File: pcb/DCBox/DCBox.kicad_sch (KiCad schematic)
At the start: 36 parts, among them J1 DC-IN, J2 Out-1, J3 Out-2, J4 Out-3, U1 STC8H1K08_TSSOP20

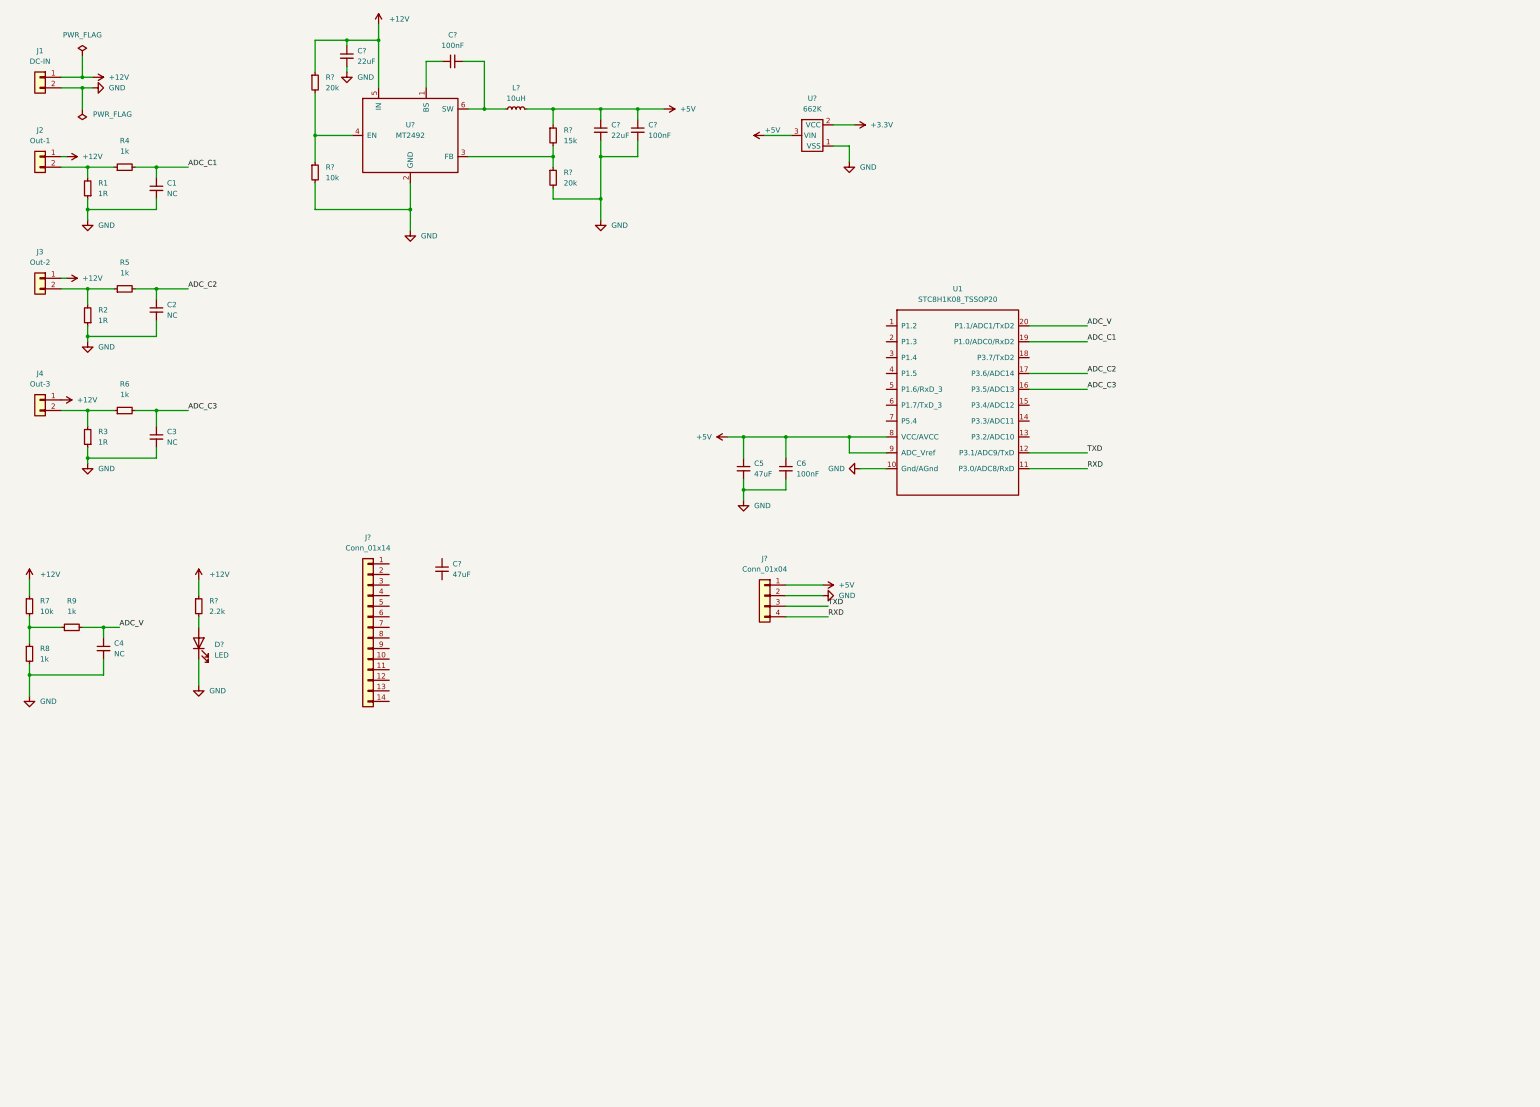
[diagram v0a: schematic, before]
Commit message: 1. 完善原理图 2. 添加显示屏datasheet
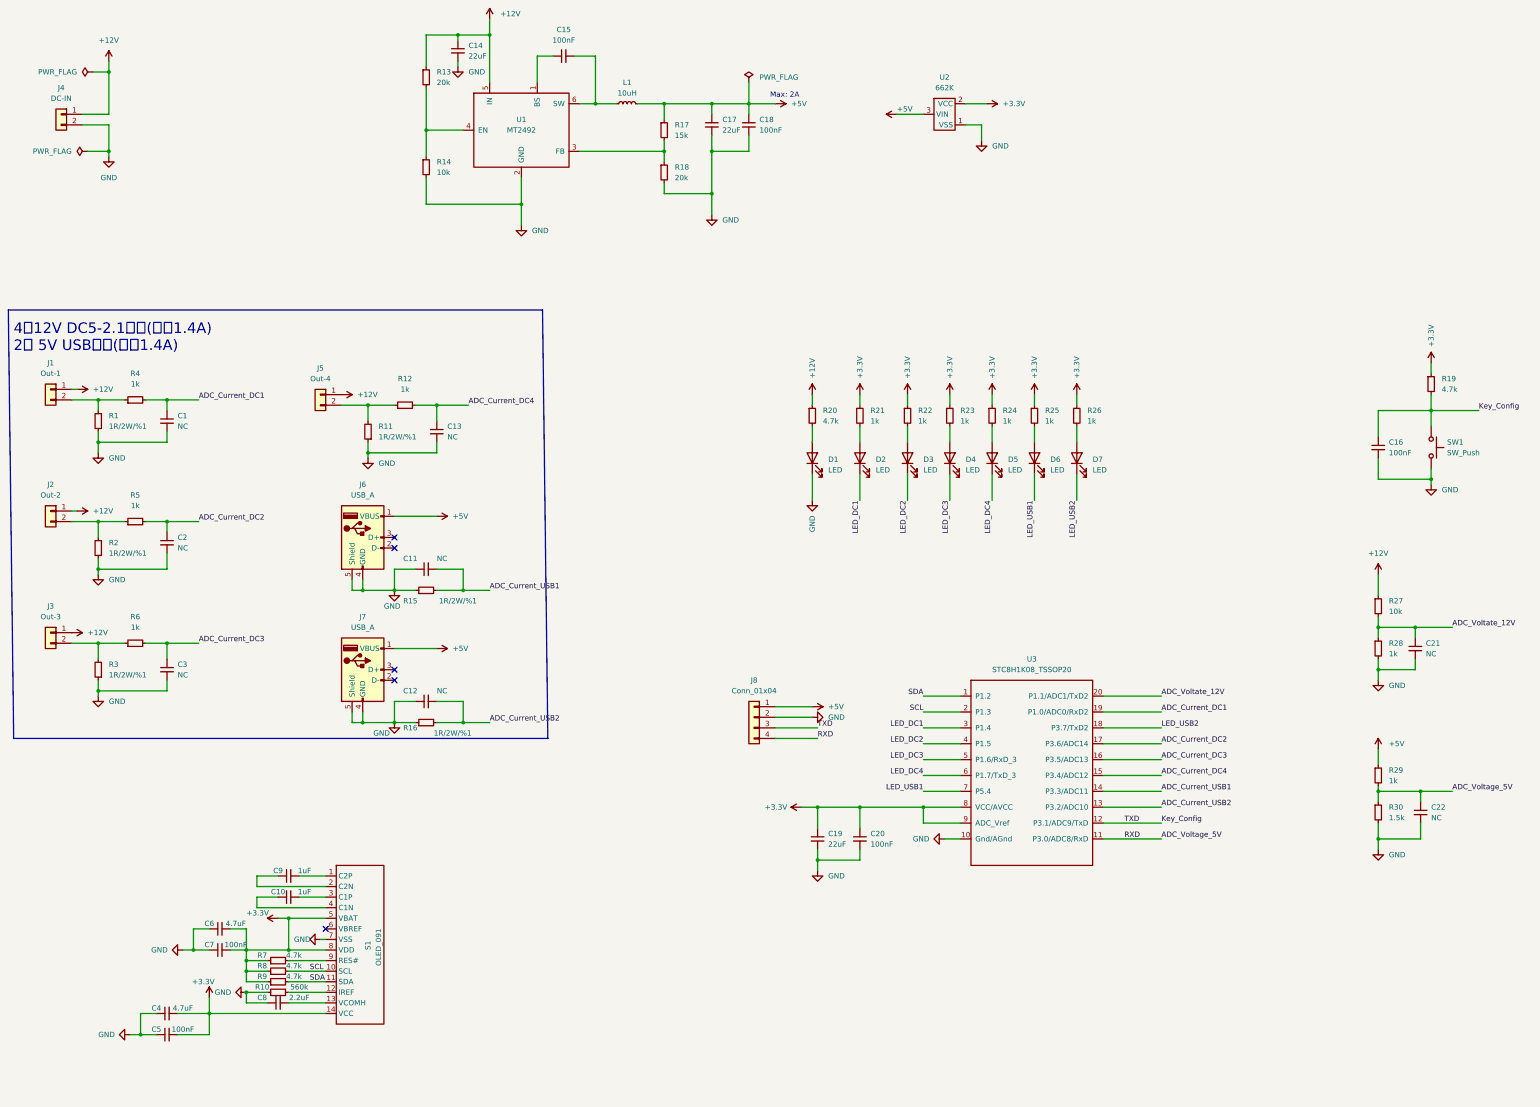
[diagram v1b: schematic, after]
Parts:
- removed C?: 47uF, symbol Device:C_Small
- removed D?: LED, symbol Device:LED
- removed J?: Conn_01x14, symbol Connector_Generic:Conn_01x14
- removed R?: 2.2k, symbol Device:R_Small
- added C10, C9: 1uF, symbol Device:C_Small
- added C11, C12, C13, C21, C22: NC, symbol Device:C_Small
- added C16, C5, C7: 100nF, symbol Device:C_Small
- added C6: 4.7uF, symbol Device:C_Small
- added C8: 2.2uF, symbol Device:C_Small
- added D1, D2, D3, D4, D5, D6, D7: LED, symbol Device:LED
- added J5: Out-4, jld:DC005, symbol Connector_Generic:Conn_01x02
- added J6, J7: USB_A, symbol Connector:USB_A
- added R10: 560k, symbol Device:R_Small
- added R11, R15, R16: 1R/2W/%1, lc_lib:2512_R, symbol Device:R_Small
- added R12, R21, R22, R23, R24, R25, R26, R28, R29: 1k, symbol Device:R_Small
- added R19, R20: 4.7k, symbol Device:R_Small
- added R27: 10k, symbol Device:R_Small
- added R30: 1.5k, symbol Device:R_Small
- added S1: OLED_091, symbol jld:OLED_091
- added SW1: SW_Push, symbol Switch:SW_Push
- C19: renamed from C5; value 47uF -> 22uF
- C4: value NC -> 4.7uF
- R1, R2, R3: value 1R -> 1R/2W/%1
- R7: value 10k -> 4.7k
- R8, R9: value 1k -> 4.7k
- gave numbers to parts that had none: 12
- renumbered C6 to C20, J2 to J1, J3 to J2, J4 to J3, J1 to J4, U1 to U3
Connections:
- net +12V: now also J5.1 (Pin_1), R20.1, R27.1; no longer R7.1
- net +3V3: now also C19.1, C20.1, C4.2, R7.1, R8.1, R9.1, U3.8 (VCC/AVCC), U3.9 (ADC_Vref), C5.2, C6.2, C7.2, R19.1, R21.1, R22.1, R23.1, R24.1, R25.1, R26.1, S1.14 (VCC), S1.5 (VBAT), S1.8 (VDD)
- net +5V: now also J6.1 (VBUS), J7.1 (VBUS), R29.1; no longer C19.1, C20.1, U3.8 (VCC/AVCC), U3.9 (ADC_Vref)
- net GND: now also C4.1, C11.1, C12.1, C13.2, C16.2, C21.2, C22.2, C5.1, C6.1, C7.1, C8.1, D1.1 (K), J6.4 (GND), J6.5 (Shield), J7.4 (GND), J7.5 (Shield), R10.1, R11.1, R15.1, R16.1, R28.2, R30.2, S1.7 (VSS), SW1.2; no longer C4.2, R8.2
- net SDA: now reaches U3.1 (P1.2)
- net SDA: now also R9.2, S1.11 (SDA)
- net ADC_Current_USB2: now reaches U3.13 (P3.2/ADC10)
- net ADC_Current_USB2: now also C12.2, R16.2
- net ADC_Current_USB1: now reaches U3.14 (P3.3/ADC11)
- net ADC_Current_USB1: now also C11.2, R15.2
- net ADC_Current_DC4: now reaches U3.15 (P3.4/ADC12)
- net ADC_Current_DC4: now also C13.1, R12.2
- net LED_USB2: now reaches U3.18 (P3.7/TxD2)
- net LED_USB2: now also D7.1 (K)
- net SCL: now reaches U3.2 (P1.3)
- net SCL: now also R8.2, S1.10 (SCL)
- net LED_DC1: now reaches U3.3 (P1.4)
- net LED_DC1: now also D2.1 (K)
- net LED_DC2: now reaches U3.4 (P1.5)
- net LED_DC2: now also D3.1 (K)
- net LED_DC3: now reaches U3.5 (P1.6/RxD_3)
- net LED_DC3: now also D4.1 (K)
- net LED_DC4: now reaches U3.6 (P1.7/TxD_3)
- net LED_DC4: now also D5.1 (K)
- net LED_USB1: now reaches U3.7 (P5.4)
- net LED_USB1: now also D6.1 (K)
- net ADC_C1 renamed ADC_Current_DC1
- net ADC_C2 renamed ADC_Current_DC2
- net ADC_C3 renamed ADC_Current_DC3
- removed net ADC_V: C4.1, R9.2, U3.20 (P1.1/ADC1/TxD2)
- net RXD renamed ADC_Voltage_5V
- net ADC_Voltage_5V: now also C22.1, R29.2, R30.1
- net TXD renamed Key_Config
- net Key_Config: now also C16.1, R19.2, SW1.1
- new net: R7.2, S1.9 (RES#)
- new net: D2.2 (A), R21.2
- new net: J5.2 (Pin_2), R11.2, R12.1
- new net: D4.2 (A), R23.2
- new net: D7.2 (A), R26.2
- new net: D1.2 (A), R20.2
- new net: D6.2 (A), R25.2
- new net: C8.2, S1.13 (VCOMH)
- new net: C9.2, S1.1 (C2P)
- new net: R10.2, S1.12 (IREF)
- new net: C9.1, S1.2 (C2N)
- new net: C10.2, S1.3 (C1P)
- new net: C10.1, S1.4 (C1N)
- new net: D3.2 (A), R22.2
- new net: D5.2 (A), R24.2
- new net ADC_Voltate_12V: C21.1, R27.2, R28.1, U3.20 (P1.1/ADC1/TxD2)
- no-connect marks 0 -> 5
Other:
- note added: "4路12V DC5-2.1输出(最大1.4A) 2路 5V USB输出(最大1.4A)"
- note added: "Max: 2A"
- moved on the sheet: C1, C14, C15, C17, C18, C19, C2, C20, C3, J1, J2, J3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

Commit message: 1. 完善布局
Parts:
- C1, C10, C11, C12, C13, C15, C16, C18, C2, C20, C21, C22, C3, C4, C5, C6, C7, C8, C9, R10, R12, R13, R14, R17, R18, R19, R20, R21, R22, R23, R24, R25, R26, R27, R28, R29, R30, R4, R5, R6, R7, R8, R9: footprint (none) -> lc_lib:0603_R
- C14, C17, C19: footprint (none) -> lc_lib:1206_R
- D1, D2, D3, D4, D5, D6, D7: footprint (none) -> lc_lib:0603_LED_N1
- J6, J7: footprint (none) -> Connector_USB:USB_A_Wuerth_614004134726_Horizontal
- J8: footprint (none) -> Connector_PinHeader_2.54mm:PinHeader_1x04_P2.54mm_Vertical
- SW1: footprint (none) -> jld:Button_SW_THT_6.2x6.2
- U1: footprint (none) -> lc_lib:SOT-23-6
- U2: footprint (none) -> lc_lib:SOT-23-3L
- U3: footprint (none) -> lc_lib:TSSOP-20
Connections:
- net ADC_Current_USB1: now also C11.1, J6.4 (GND), J6.5 (Shield), R15.1; no longer C11.2, R15.2
- net ADC_Current_USB2: now also C12.1, J7.4 (GND), J7.5 (Shield), R16.1; no longer C12.2, R16.2
- net GND: now also C11.2, C12.2, R15.2, R16.2; no longer C11.1, C12.1, J6.4 (GND), J6.5 (Shield), J7.4 (GND), J7.5 (Shield), R15.1, R16.1

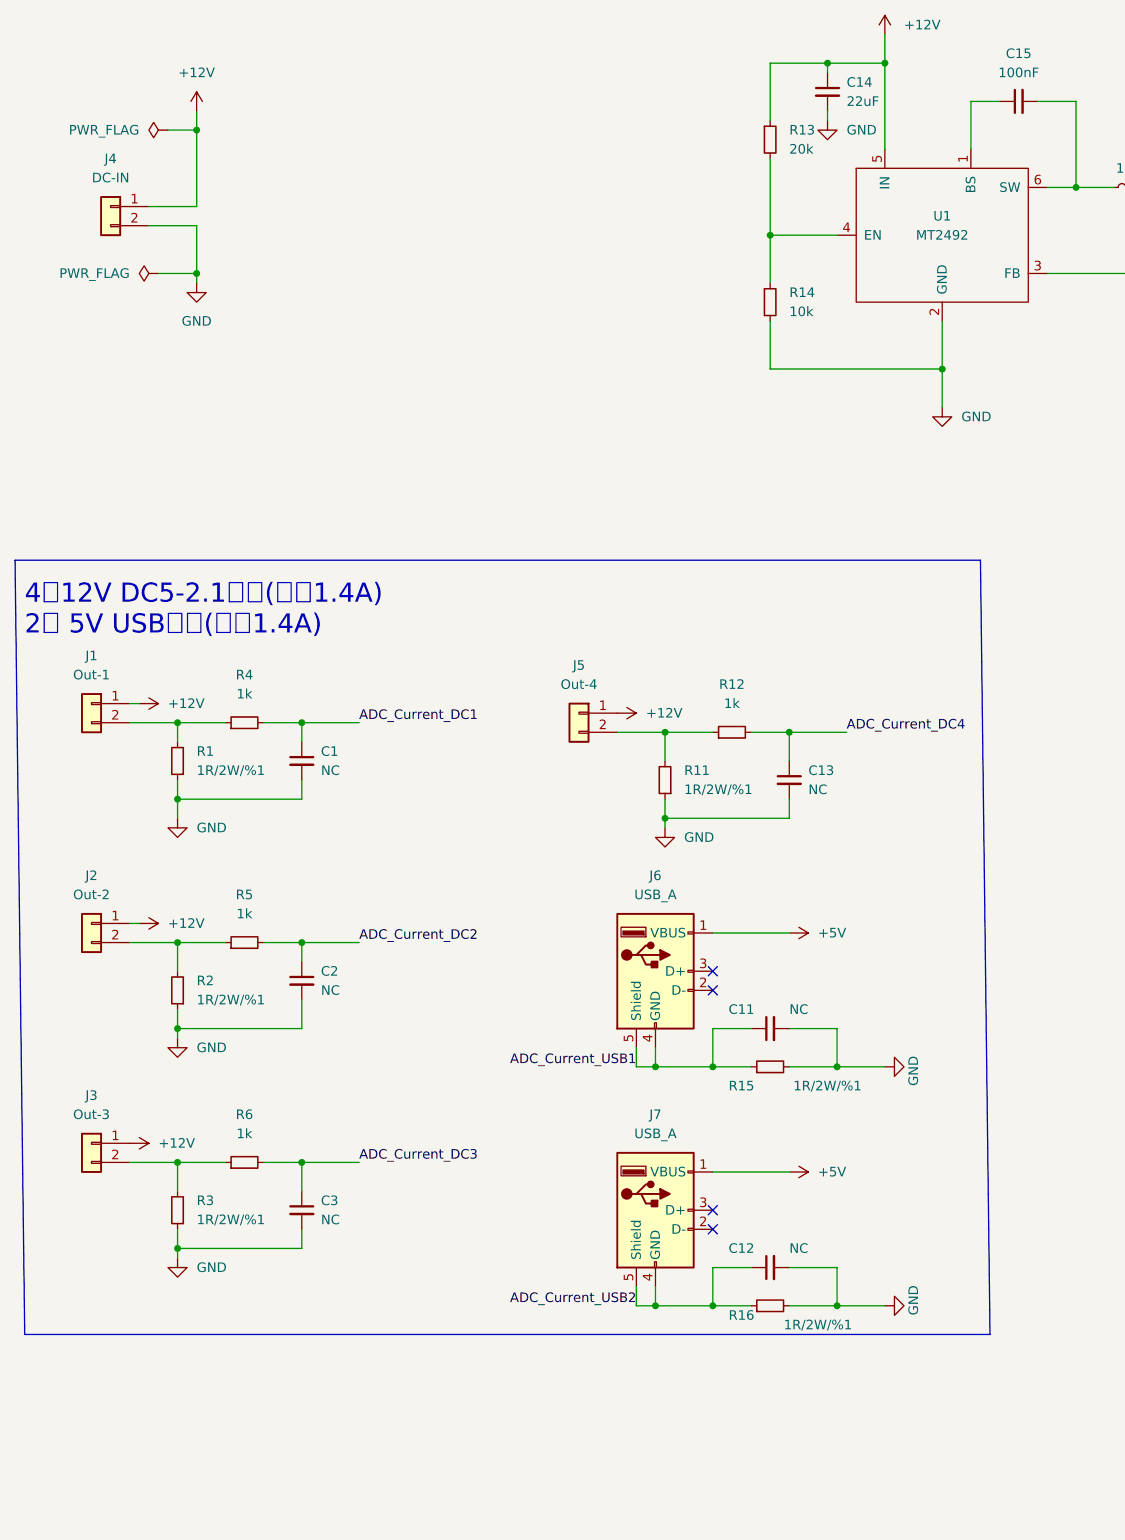
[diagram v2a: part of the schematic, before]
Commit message: 1. 进线DC增加可恢复保险丝 2. 布局完善
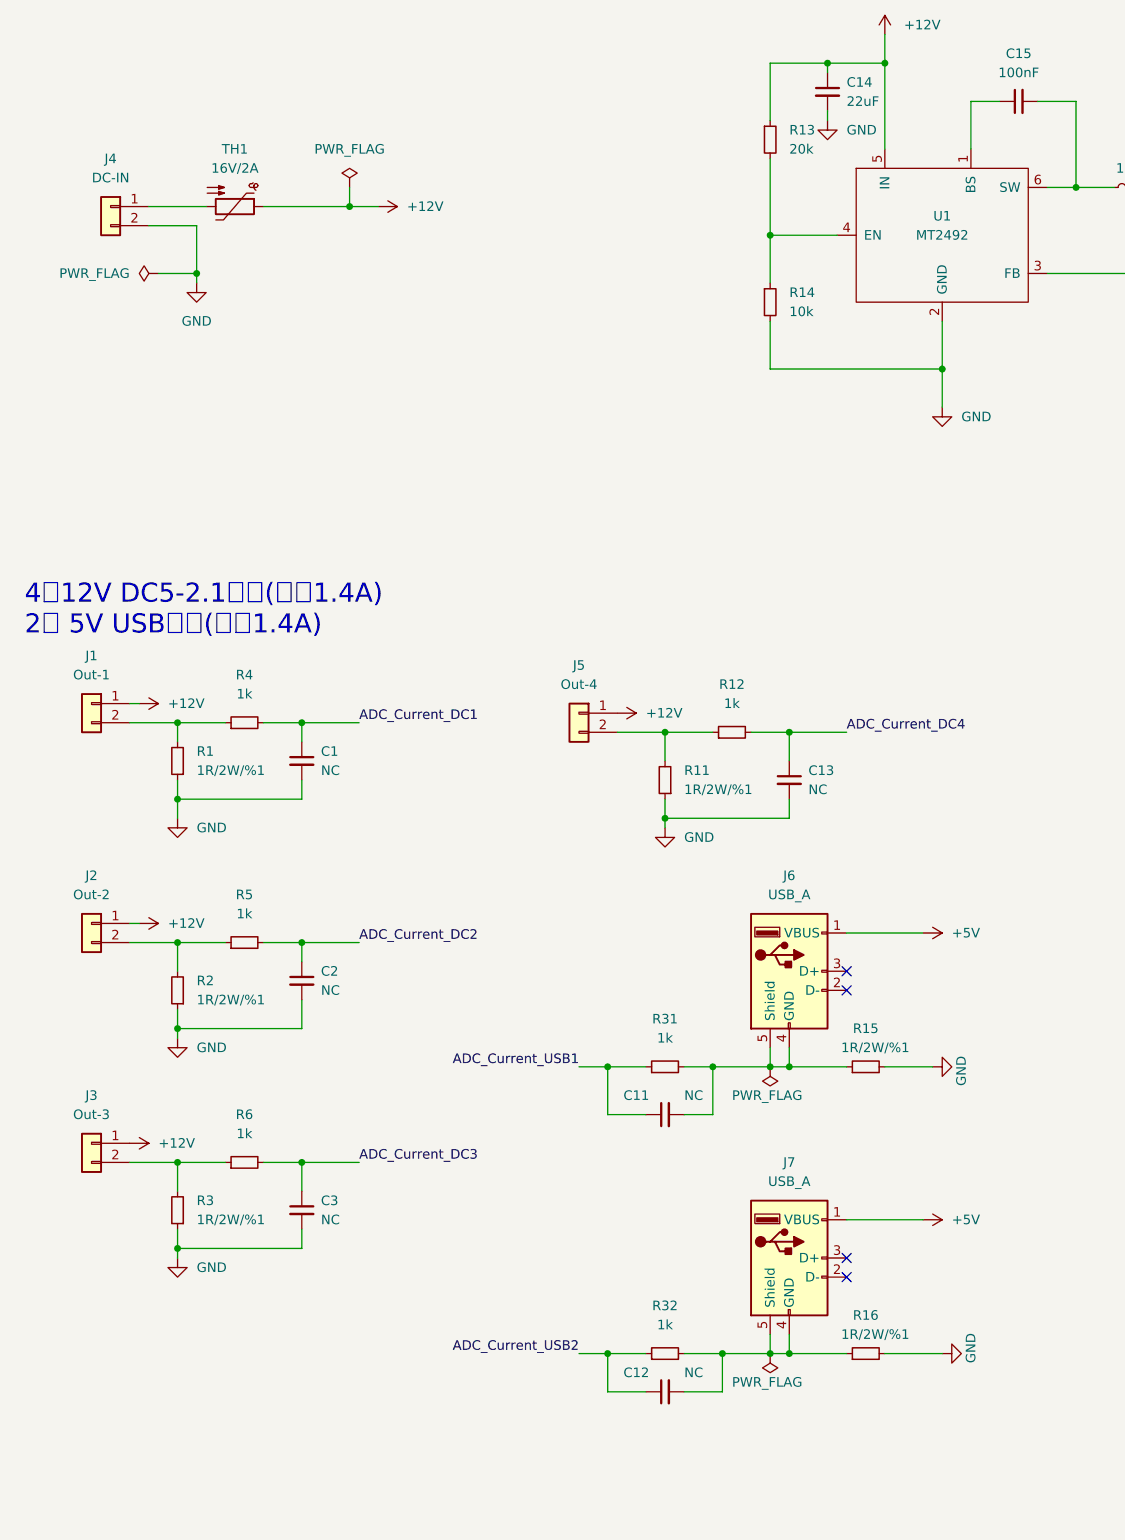
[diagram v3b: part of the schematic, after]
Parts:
- added R31, R32: 1k, lc_lib:0603_R, symbol Device:R_Small
- added TH1: 16V/2A, lc_lib:1812_R, symbol Device:Thermistor_PTC
- L1: footprint (none) -> Inductor_SMD:L_Bourns-SRN6028
- S1: footprint (none) -> jld:ZJY09_Screen
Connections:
- net +12V: now also TH1.1; no longer J4.1 (Pin_1)
- net ADC_Current_USB1: now also R31.1; no longer J6.4 (GND), J6.5 (Shield), R15.1
- net ADC_Current_USB2: now also R32.1; no longer J7.4 (GND), J7.5 (Shield), R16.1
- net GND: no longer C11.2, C12.2
- new net: C11.2, J6.4 (GND), J6.5 (Shield), R15.1, R31.2
- new net: C12.2, J7.4 (GND), J7.5 (Shield), R16.1, R32.2
- new net: J4.1 (Pin_1), TH1.2
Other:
- moved on the sheet: C11, C12, J6, J7, R15, R16
